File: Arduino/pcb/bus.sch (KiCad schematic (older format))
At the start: 4 parts, among them J2 Floppy-Bus, J3 MAX485 Socket, J4 Floppy-Bus

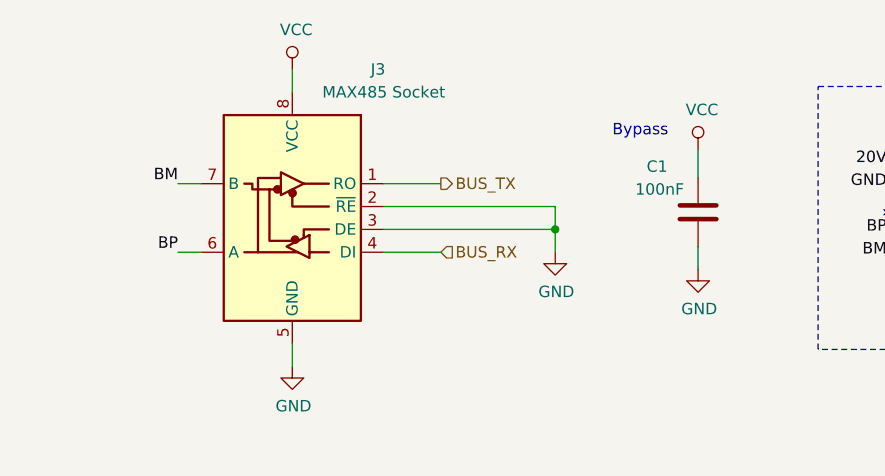
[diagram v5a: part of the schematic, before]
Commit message: pcb: route RS485 control pins
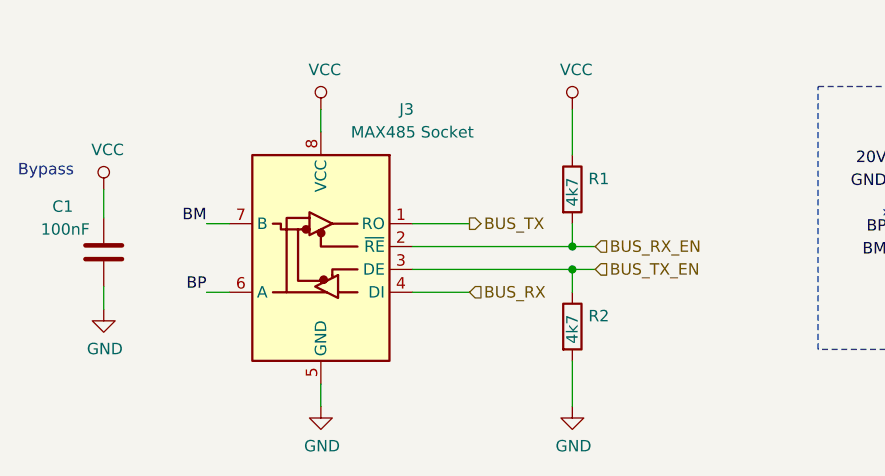
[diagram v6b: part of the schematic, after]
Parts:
- added R1, R2: 4k7, Resistor_SMD:R_0805_2012Metric, symbol Device:R
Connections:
- net GND: now also R2.2; no longer J3.2 (~RE), J3.3 (DE)
- net VCC: now also R1.1
- new net BUS_RX_EN: J3.2 (~RE), R1.2
- new net BUS_TX_EN: J3.3 (DE), R2.1
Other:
- moved on the sheet: C1, J3
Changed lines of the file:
@@
 $Descr A4 11693 8268
 encoding utf-8
-Sheet 2 6
+Sheet 5 6
 Title ""
 Date ""
@@
 L Interface_UART:MAX485E J3
 U 1 1 5CF1EB96
-P 4750 1400
-F 0 "J3" H 4375 2000 50  0000 C CNN
-F 1 "MAX485 Socket" H 4350 1900 50  0000 C CNN
-F 2 "dil:dil_8-300_socket" H 4750 1400 50  0001 C CNN
-F 3 "" H 4750 1400 50  0001 C CNN
-	1    4750 1400
+P 4875 1575
+F 0 "J3" H 4500 2175 50  0000 C CNN
+F 1 "MAX485 Socket" H 4475 2075 50  0000 C CNN
+F 2 "dil:dil_8-300_socket" H 4875 1575 50  0001 C CNN
+F 3 "" H 4875 1575 50  0001 C CNN
+	1    4875 1575
 	-1   0    0    -1
 $EndComp
@@
 L power:VCC #PWR04
 U 1 1 5CF1EBBB
-P 4750 800
-F 0 "#PWR04" H 4750 650 50  0001 C CNN
-F 1 "VCC" H 4767 973 50  0000 C CNN
-F 2 "" H 4750 800 50  0001 C CNN
-F 3 "" H 4750 800 50  0001 C CNN
-	1    4750 800
+P 4875 975
+F 0 "#PWR04" H 4875 825 50  0001 C CNN
+F 1 "VCC" H 4892 1148 50  0000 C CNN
+F 2 "" H 4875 975 50  0001 C CNN
+F 3 "" H 4875 975 50  0001 C CNN
+	1    4875 975
 	1    0    0    -1
 $EndComp
@@
 L power:GND #PWR05
 U 1 1 5CF1EBC1
-P 4750 2100
-F 0 "#PWR05" H 4750 1850 50  0001 C CNN
-F 1 "GND" H 4755 1927 50  0000 C CNN
-F 2 "" H 4750 2100 50  0001 C CNN
-F 3 "" H 4750 2100 50  0001 C CNN
-	1    4750 2100
-	1    0    0    -1
-$EndComp
-Wire Wire Line
-	4750 900  4750 800
-Wire Wire Line
-	4750 2000 4750 2100
-Wire Wire Line
-	5150 1300 5400 1300
-Wire Wire Line
-	5150 1600 5400 1600
-Wire Wire Line
-	5150 1500 5900 1500
-Wire Wire Line
-	5150 1400 5900 1400
-Wire Wire Line
-	5900 1400 5900 1500
-Connection ~ 5900 1500
-$Comp
-L power:GND #PWR07
-U 1 1 5CF1EBD6
-P 5900 1600
-F 0 "#PWR07" H 5900 1350 50  0001 C CNN
-F 1 "GND" H 5905 1427 50  0000 C CNN
-F 2 "" H 5900 1600 50  0001 C CNN
-F 3 "" H 5900 1600 50  0001 C CNN
-	1    5900 1600
-	1    0    0    -1
-$EndComp
-Wire Wire Line
-	5900 1500 5900 1600
-Text HLabel 5400 1300 2    50   Output ~ 0
+P 4875 2275
+F 0 "#PWR05" H 4875 2025 50  0001 C CNN
+F 1 "GND" H 4880 2102 50  0000 C CNN
+F 2 "" H 4875 2275 50  0001 C CNN
+F 3 "" H 4875 2275 50  0001 C CNN
+	1    4875 2275
+	1    0    0    -1
+$EndComp
+Wire Wire Line
+	4875 1075 4875 975
+Wire Wire Line
+	4875 2175 4875 2275
+Wire Wire Line
+	5275 1475 5525 1475
+Wire Wire Line
+	5275 1775 5525 1775
+Text HLabel 5525 1475 2    50   Output ~ 0
 BUS_TX
-Text HLabel 5400 1600 2    50   Input ~ 0
+Text HLabel 5525 1775 2    50   Input ~ 0
 BUS_RX
 Text HLabel 10700 1300 0    50   Output ~ 0
@@
 L Device:C C?
 U 1 1 5D17F33C
-P 6525 1425
+P 3925 1600
 AR Path="/5D17F33C" Ref="C?"  Part="1"
 AR Path="/5CCFEC3E/5D17F33C" Ref="C?"  Part="1"
 AR Path="/5CD1E0A5/5D17F33C" Ref="C1"  Part="1"
-F 0 "C1" H 6300 1625 50  0000 L CNN
-F 1 "100nF" H 6250 1525 50  0000 L CNN
-F 2 "Capacitor_SMD:C_0805_2012Metric" H 6563 1275 50  0001 C CNN
-F 3 "~" H 6525 1425 50  0001 C CNN
-	1    6525 1425
+F 0 "C1" H 3700 1800 50  0000 L CNN
+F 1 "100nF" H 3650 1700 50  0000 L CNN
+F 2 "Capacitor_SMD:C_0805_2012Metric" H 3963 1450 50  0001 C CNN
+F 3 "~" H 3925 1600 50  0001 C CNN
+	1    3925 1600
 	1    0    0    -1
 $EndComp
@@
 L power:VCC #PWR?
 U 1 1 5D17F342
-P 6525 1150
+P 3925 1325
 AR Path="/5CCFEC3E/5D17F342" Ref="#PWR?"  Part="1"
 AR Path="/5CD1E0A5/5D17F342" Ref="#PWR02"  Part="1"
-F 0 "#PWR02" H 6525 1000 50  0001 C CNN
-F 1 "VCC" H 6542 1323 50  0000 C CNN
-F 2 "" H 6525 1150 50  0001 C CNN
-F 3 "" H 6525 1150 50  0001 C CNN
-	1    6525 1150
+F 0 "#PWR02" H 3925 1175 50  0001 C CNN
+F 1 "VCC" H 3942 1498 50  0000 C CNN
+F 2 "" H 3925 1325 50  0001 C CNN
+F 3 "" H 3925 1325 50  0001 C CNN
+	1    3925 1325
 	1    0    0    -1
 $EndComp
@@
 L power:GND #PWR?
 U 1 1 5D17F348
-P 6525 1675
+P 3925 1850
 AR Path="/5CCFEC3E/5D17F348" Ref="#PWR?"  Part="1"
 AR Path="/5CD1E0A5/5D17F348" Ref="#PWR03"  Part="1"
-F 0 "#PWR03" H 6525 1425 50  0001 C CNN
-F 1 "GND" H 6530 1502 50  0000 C CNN
-F 2 "" H 6525 1675 50  0001 C CNN
-F 3 "" H 6525 1675 50  0001 C CNN
-	1    6525 1675
-	1    0    0    -1
-$EndComp
-Wire Wire Line
-	6525 1150 6525 1275
-Wire Wire Line
-	6525 1575 6525 1675
-Text Notes 6150 1100 0    50   ~ 0
+F 0 "#PWR03" H 3925 1600 50  0001 C CNN
+F 1 "GND" H 3930 1677 50  0000 C CNN
+F 2 "" H 3925 1850 50  0001 C CNN
+F 3 "" H 3925 1850 50  0001 C CNN
+	1    3925 1850
+	1    0    0    -1
+$EndComp
+Wire Wire Line
+	3925 1325 3925 1450
+Wire Wire Line
+	3925 1750 3925 1850
+Text Notes 3550 1275 0    50   ~ 0
 Bypass
 $Comp
@@
 Text Label 10900 1300 0    50   ~ 0
 20V
-Text Label 4250 1600 2    50   ~ 0
-BP
-Text Label 4250 1300 2    50   ~ 0
+Text Label 4375 1775 2    50   ~ 0
+BP
+Text Label 4375 1475 2    50   ~ 0
 BM
 Wire Wire Line
@@
 	10800 1200 10800 1300
 Wire Wire Line
-	4350 1300 4250 1300
-Wire Wire Line
-	4350 1600 4250 1600
+	4475 1475 4375 1475
+Wire Wire Line
+	4475 1775 4375 1775
 Text Label 7350 1225 2    50   ~ 0
 20V
@@
 Wire Notes Line
 	10075 875  10075 2025
+Text HLabel 6075 1575 2    50   Input ~ 0
+BUS_RX_EN
+Text HLabel 6075 1675 2    50   Input ~ 0
+BUS_TX_EN
+$Comp
+L Device:R R1
+U 1 1 5D9A9AF7
+P 5975 1325
+F 0 "R1" H 6045 1371 50  0000 L CNN
+F 1 "4k7" V 5975 1250 50  0000 L CNN
+F 2 "Resistor_SMD:R_0805_2012Metric" V 5905 1325 50  0001 C CNN
+F 3 "~" H 5975 1325 50  0001 C CNN
+	1    5975 1325
+	1    0    0    -1
+$EndComp
+$Comp
+L Device:R R2
+U 1 1 5D9A9F68
+P 5975 1925
+F 0 "R2" H 6045 1971 50  0000 L CNN
+F 1 "4k7" V 5975 1850 50  0000 L CNN
+F 2 "Resistor_SMD:R_0805_2012Metric" V 5905 1925 50  0001 C CNN
+F 3 "~" H 5975 1925 50  0001 C CNN
+	1    5975 1925
+	1    0    0    -1
+$EndComp
+Wire Wire Line
+	5275 1575 5975 1575
+Wire Wire Line
+	5275 1675 5975 1675
+Wire Wire Line
+	5975 1575 5975 1475
+Wire Wire Line
+	5975 1575 6075 1575
+Connection ~ 5975 1575
+Wire Wire Line
+	5975 1675 5975 1775
+Wire Wire Line
+	5975 1675 6075 1675
+Connection ~ 5975 1675
+$Comp
+L power:VCC #PWR0105
+U 1 1 5D9C25C7
+P 5975 975
+F 0 "#PWR0105" H 5975 825 50  0001 C CNN
+F 1 "VCC" H 5992 1148 50  0000 C CNN
+F 2 "" H 5975 975 50  0001 C CNN
+F 3 "" H 5975 975 50  0001 C CNN
+	1    5975 975
+	1    0    0    -1
+$EndComp
+$Comp
+L power:GND #PWR0106
+U 1 1 5D9C302F
+P 5975 2275
+F 0 "#PWR0106" H 5975 2025 50  0001 C CNN
+F 1 "GND" H 5980 2102 50  0000 C CNN
+F 2 "" H 5975 2275 50  0001 C CNN
+F 3 "" H 5975 2275 50  0001 C CNN
+	1    5975 2275
+	1    0    0    -1
+$EndComp
+Wire Wire Line
+	5975 2075 5975 2275
+Wire Wire Line
+	5975 975  5975 1175
 $EndSCHEMATC

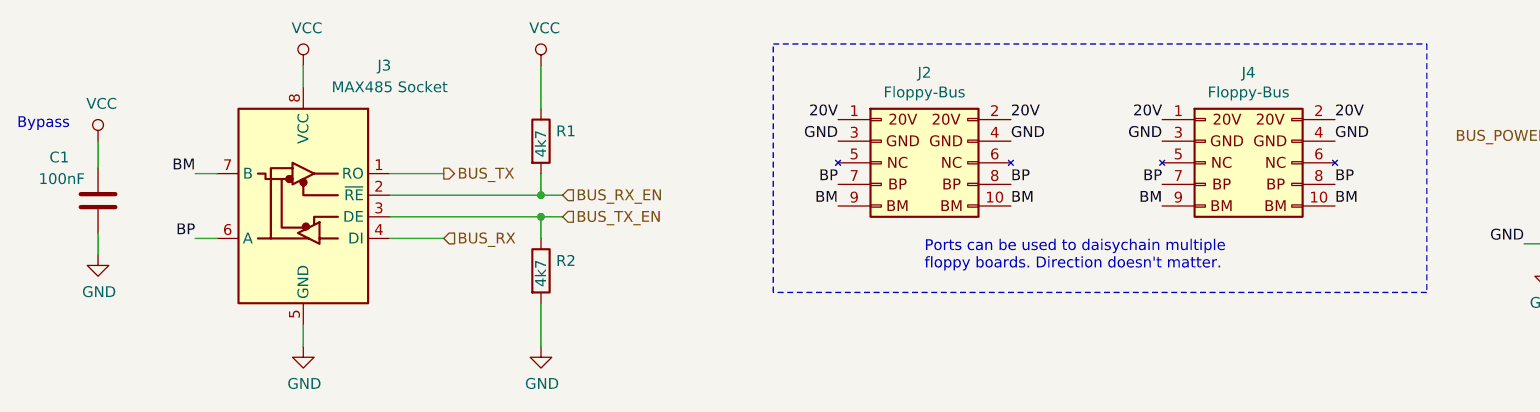
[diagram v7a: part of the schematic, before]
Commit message: pcb: rename RS485 bus pins + differential pair routing
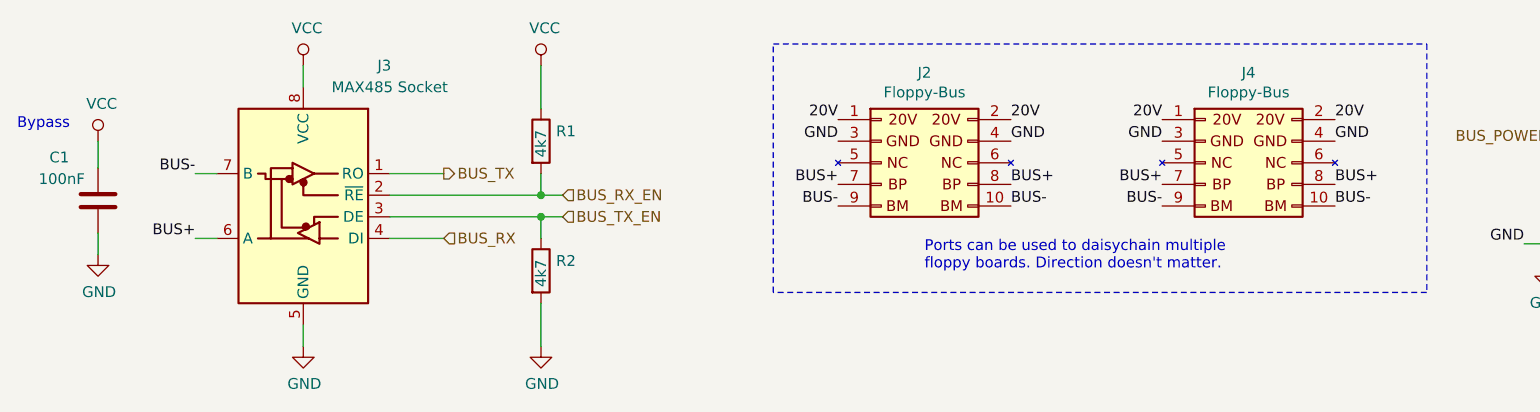
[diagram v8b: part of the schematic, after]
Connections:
- net BM renamed BUS-
- net BP renamed BUS+
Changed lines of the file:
@@
 Text Label 10900 1300 0    50   ~ 0
 20V
-Text Label 4375 1775 2    50   ~ 0
-BP
-Text Label 4375 1475 2    50   ~ 0
-BM
 Wire Wire Line
 	10900 1300 10800 1300
@@
 	1    0    0    -1
 $EndComp
-Text Label 7350 1525 2    50   ~ 0
-BP
-Text Label 7350 1625 2    50   ~ 0
-BM
-Text Label 8150 1525 0    50   ~ 0
-BP
-Text Label 9650 1525 0    50   ~ 0
-BP
-Text Label 8850 1525 2    50   ~ 0
-BP
-Text Label 8850 1625 2    50   ~ 0
-BM
-Text Label 8150 1625 0    50   ~ 0
-BM
-Text Label 9650 1625 0    50   ~ 0
-BM
 Text Notes 7750 1925 0    50   ~ 0
 Ports can be used to daisychain multiple\nfloppy boards. Direction doesn't matter.
@@
 Wire Wire Line
 	5975 975  5975 1175
+Text Label 4375 1475 2    50   ~ 0
+BUS-
+Text Label 4375 1775 2    50   ~ 0
+BUS+
+Text Label 7350 1525 2    50   ~ 0
+BUS+
+Text Label 7350 1625 2    50   ~ 0
+BUS-
+Text Label 8150 1525 0    50   ~ 0
+BUS+
+Text Label 8150 1625 0    50   ~ 0
+BUS-
+Text Label 8850 1525 2    50   ~ 0
+BUS+
+Text Label 8850 1625 2    50   ~ 0
+BUS-
+Text Label 9650 1525 0    50   ~ 0
+BUS+
+Text Label 9650 1625 0    50   ~ 0
+BUS-
 $EndSCHEMATC
